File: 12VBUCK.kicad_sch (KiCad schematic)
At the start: 1 part, among them U2 LM76005RNPR

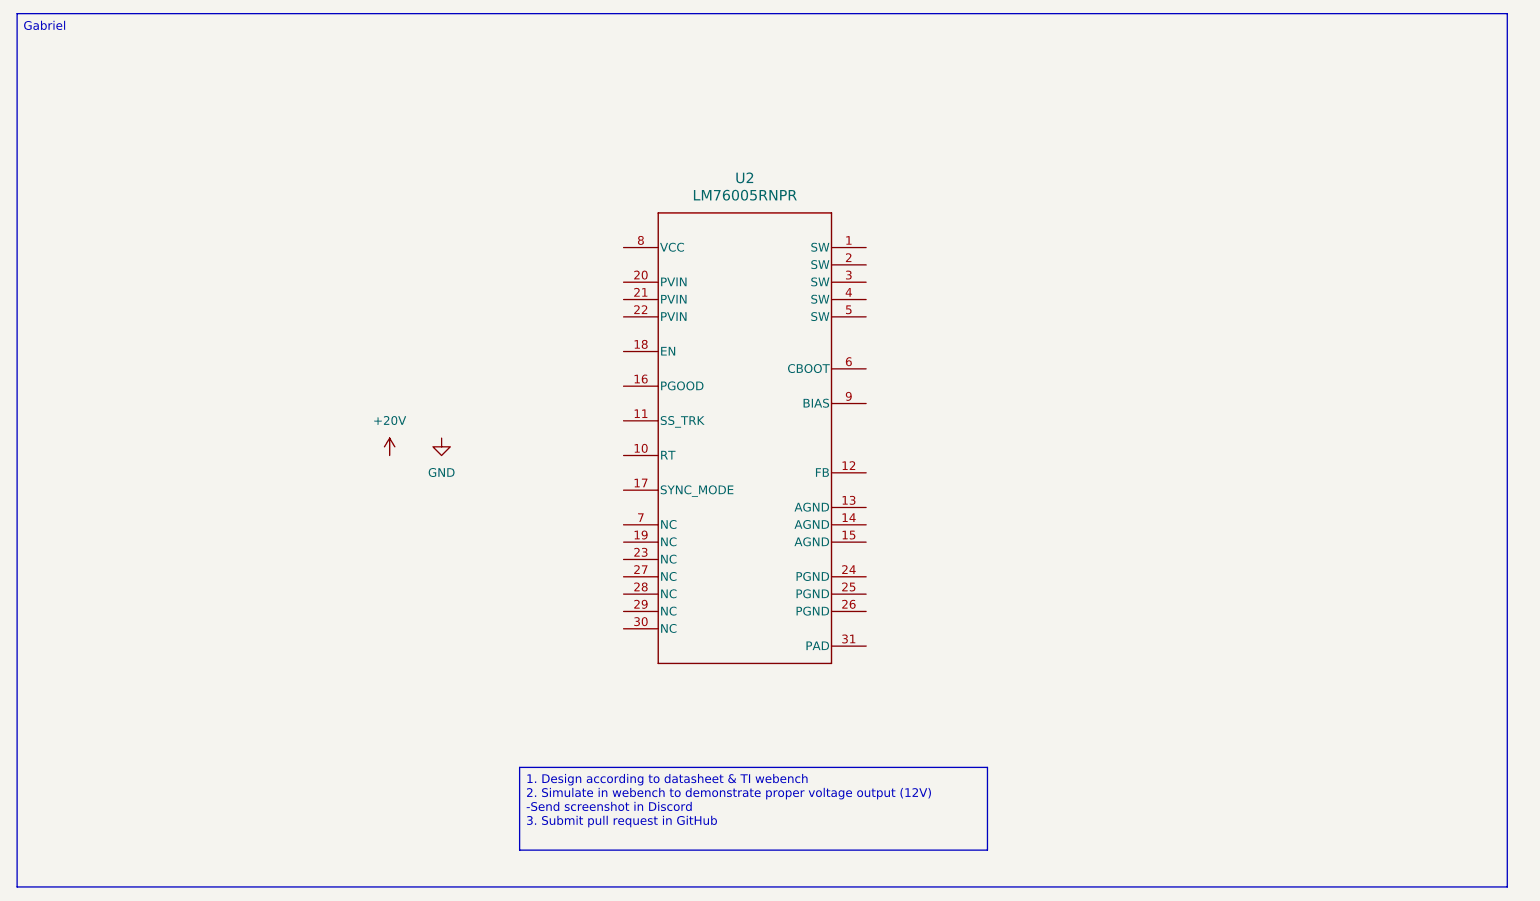
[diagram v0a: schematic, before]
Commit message: Finished 12V Buck Converter KiCad Schematic
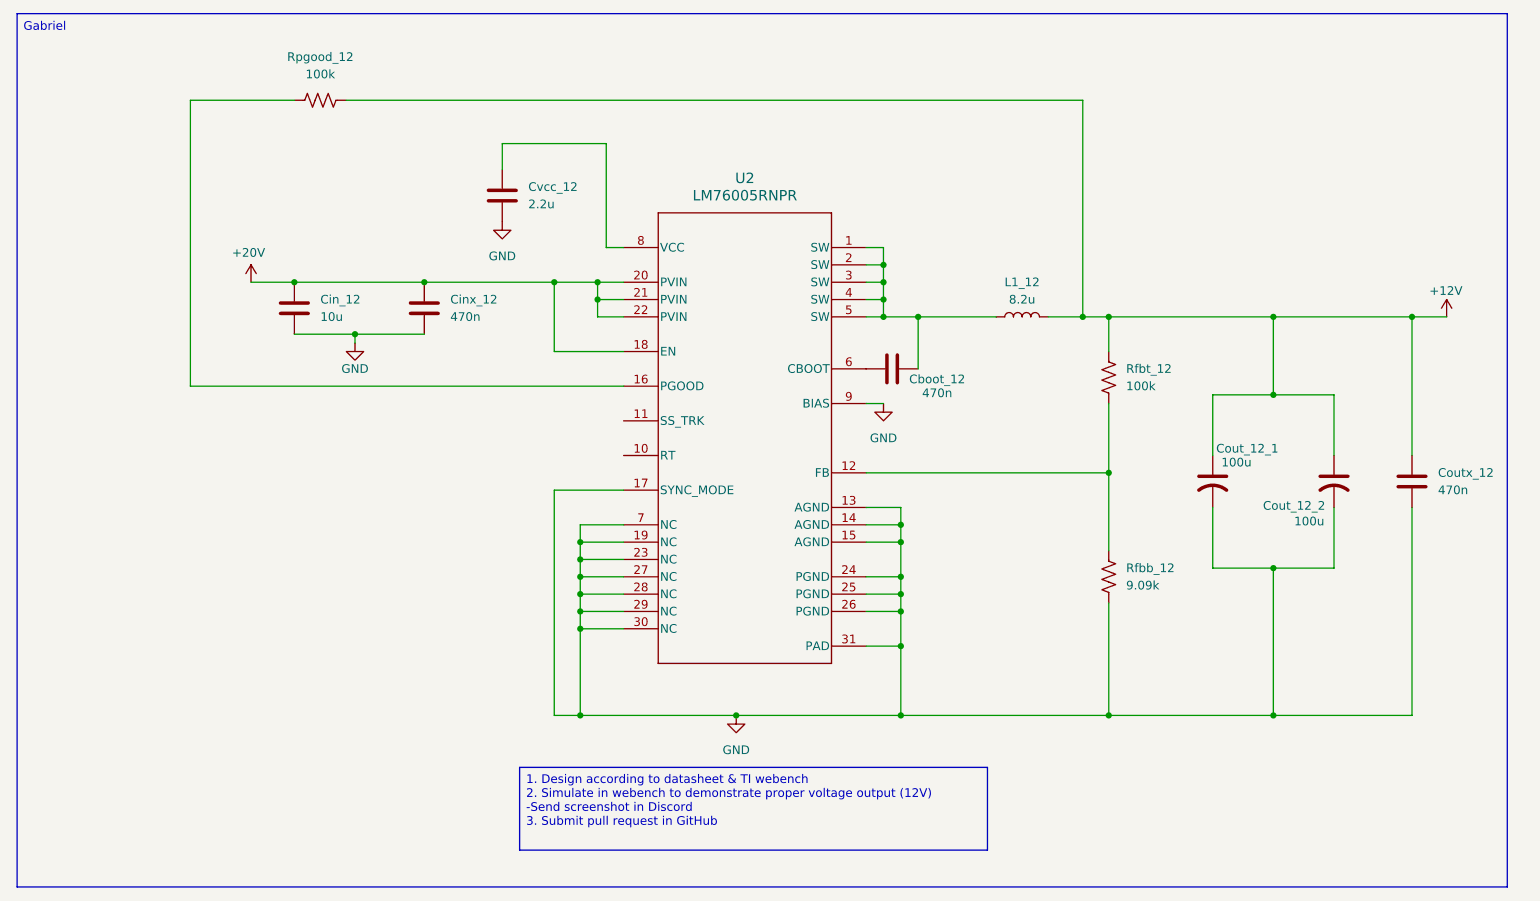
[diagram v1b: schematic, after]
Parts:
- added Cboot_12, Cinx_12, Coutx_12: 470n, Package_DIP:DIP-8_W7.62mm, symbol Device:C
- added Cin_12: 10u, Package_DIP:DIP-8_W7.62mm, symbol Device:C
- added Cout_12_1, Cout_12_2: 100u, Package_DIP:DIP-8_W7.62mm, symbol Device:C_US
- added Cvcc_12: 2.2u, Package_DIP:DIP-8_W7.62mm, symbol Device:C
- added L1_12: 8.2u, symbol Device:L
- added Rfbb_12: 9.09k, symbol Device:R_US
- added Rfbt_12, Rpgood_12: 100k, symbol Device:R_US
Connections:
- net +20V: now also U2.18 (EN), U2.20 (PVIN), U2.21 (PVIN), U2.22 (PVIN), Cin_12.1, Cinx_12.1
- net GND: now also U2.13 (AGND), U2.14 (AGND), U2.15 (AGND), U2.17 (SYNC_MODE), U2.19 (NC), U2.23 (NC), U2.24 (PGND), U2.25 (PGND), U2.26 (PGND), U2.27 (NC), U2.28 (NC), U2.29 (NC), U2.30 (NC), U2.31 (PAD), U2.7 (NC), U2.9 (BIAS), Cin_12.2, Cinx_12.2, Cout_12_1.2, Cout_12_2.2, Coutx_12.2, Cvcc_12.2, Rfbb_12.1
- net at U2.1 (SW): now also U2.2 (SW), U2.3 (SW), U2.4 (SW), U2.5 (SW), Cboot_12.1, L1_12.1
- net at U2.12 (FB): now also Rfbb_12.2, Rfbt_12.1
- net at U2.16 (PGOOD): now also Rpgood_12.1
- net at U2.6 (CBOOT): now also Cboot_12.2
- net at U2.8 (VCC): now also Cvcc_12.1
- new net +12V: Cout_12_1.1, Cout_12_2.1, Coutx_12.1, L1_12.2, Rfbt_12.2, Rpgood_12.2

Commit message: Add complete layout-ready project files
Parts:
- removed Cout_12_1, Cout_12_2: 100u, Package_DIP:DIP-8_W7.62mm, symbol Device:C_US
- added Cout_12V_1, Cout_12V_2: 100u, BulkCapacitor_100u:CAP_EEFK_F_PAN, symbol BulkCap_100u:EEE-FP1V101AP
- Cboot_12V1: renamed from Cboot_12; footprint Package_DIP:DIP-8_W7.62mm -> Capacitor_SMD:C_0805_2012Metric
- Cin_12V1: renamed from Cin_12; footprint Package_DIP:DIP-8_W7.62mm -> Capacitor_SMD:C_0805_2012Metric
- Cinx_12V1: renamed from Cinx_12; footprint Package_DIP:DIP-8_W7.62mm -> Capacitor_SMD:C_0805_2012Metric
- Coutx_12V1: renamed from Coutx_12; footprint Package_DIP:DIP-8_W7.62mm -> Capacitor_SMD:C_0805_2012Metric
- Cvcc_12V1: renamed from Cvcc_12; footprint Package_DIP:DIP-8_W7.62mm -> Capacitor_SMD:C_0603_1608Metric
- L1_12V1: renamed from L1_12; footprint (none) -> Inductor_SMD:L_Bourns_SRP7028A_7.3x6.6mm
- Rfbb_12V1: renamed from Rfbb_12; footprint (none) -> Resistor_SMD:R_0603_1608Metric
- Rfbt_12V1: renamed from Rfbt_12; footprint (none) -> Resistor_SMD:R_0603_1608Metric
- Rpgood_12V1: renamed from Rpgood_12; footprint (none) -> Resistor_SMD:R_0603_1608Metric
- U4: renamed from U2; footprint RNP0030A -> Regulator:RNP0030A
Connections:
- net +12V: now also Cout_12V_1.1, Cout_12V_2.1
- net GND: now also Cout_12V_1.2, Cout_12V_2.2
- no-connect marks 0 -> 2
